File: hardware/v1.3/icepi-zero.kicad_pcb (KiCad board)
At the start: 4 copper layers, 65 x 30 mm, 165 parts, among them J1 Conn_02x20_Counter_Clockwise, J2 GPDI_C_1.3, J3 USB_C_Receptacle_USB2.0_14P, J4 USB_C_Receptacle_USB2.0_14P, J5 USB_C_Receptacle_USB2.0_14P, J6 Micro_SD_Card_Det2, SW1 SW_Push, SW2 SW_Push, U1 ECP5-CABGA256, U10 TPD2EUSB30A, U11 W9825G6KH, U12 W25Q128JVS, U2 TLV62569DBV, U3 TLV62569DBV, U4 TLV62569DBV, U5 TPD2EUSB30A, U6 PCA9306DC1, U7 TPD2EUSB30A, U8 TPD2EUSB30A, U9 FT231XQ, Y1 SG-8018CG 50.000000MHz

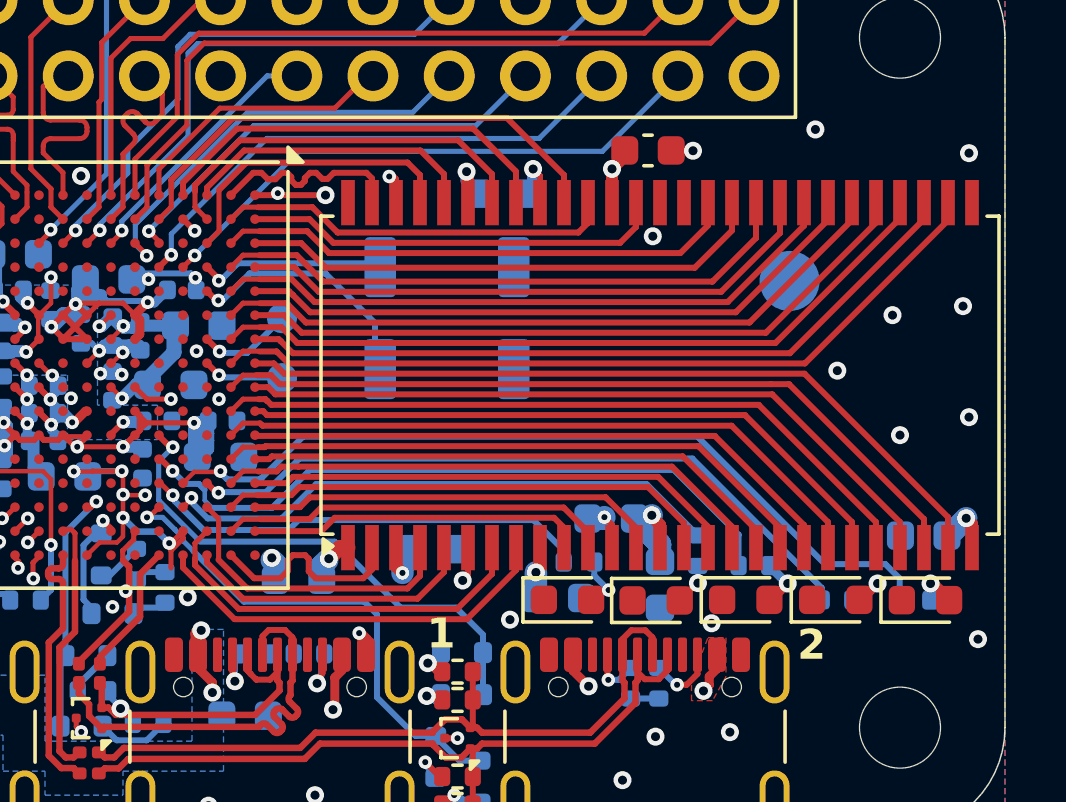
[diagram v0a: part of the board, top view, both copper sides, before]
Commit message: Replaced memory AS4C16M16SA 54-TFBGA (8x8)
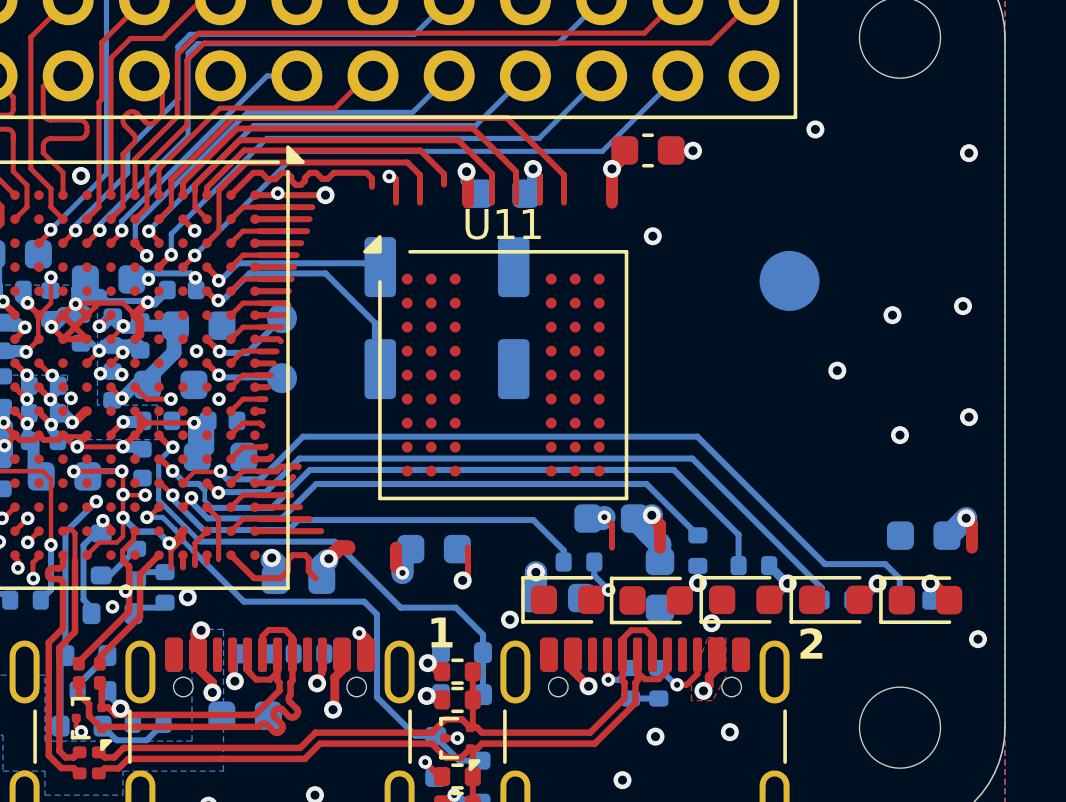
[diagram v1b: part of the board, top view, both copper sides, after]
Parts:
- L1, L2, L3: value 2.2uH 100mA+ 400mO- -> 2.2uH
- U11: value W9825G6KH -> AS4C16M16SA; footprint Package_SO:TSOP-II-54_22.2x10.16mm_P0.8mm -> Package_BGA:Alliance_TFBGA-54_8x8mm_Layout9x9_P0.8mm
- moved U11 5.22 mm to (164.3, 104.8), turned to 0 degrees
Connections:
- net DONE renamed /Flash/DONE
- net INITN renamed /Flash/INITN
- net PROGRAMMING renamed /Flash/PROGRAMMING
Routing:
- net /SDRAM/A3: track 26.2 -> 0.62 mm
- net /SDRAM/A2: track 26.3 -> 1.60 mm
- net /SDRAM/A4: track 26.2 -> 1.64 mm
- net /SDRAM/A1: track 24.2 -> 0.44 mm
- net /SDRAM/A5: track 24.3 -> 0.79 mm
- net /SDRAM/A0: track 24.2 -> 1.34 mm
- net /SDRAM/A6: track 24.4 -> 1.83 mm
- net /SDRAM/A7: track 23.1 -> 0.97 mm
- net /SDRAM/A10: track 22.3 -> 0.27 mm
- net /SDRAM/BA1: track 22.3 -> 1.24 mm
- net /SDRAM/A8: track 22.5 -> 2.08 mm
- net /SDRAM/BA0: track 20.3 -> 0.00 mm
- net /SDRAM/A9: track 20.7 -> 1.13 mm
- net /SDRAM/A11: track 21.4 -> 2.17 mm
- net /SDRAM/~{CS}: track 20.3 -> 1.38 mm
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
